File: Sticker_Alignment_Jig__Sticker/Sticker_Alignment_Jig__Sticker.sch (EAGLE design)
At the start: 5 parts

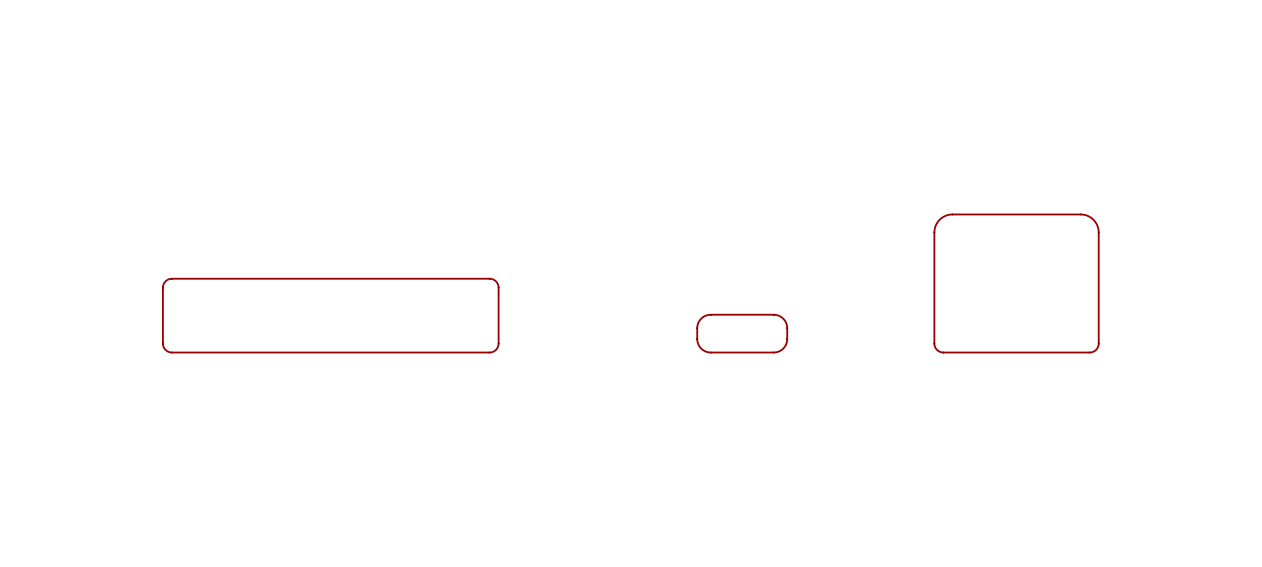
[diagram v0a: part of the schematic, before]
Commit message: Update sticker alignment jig
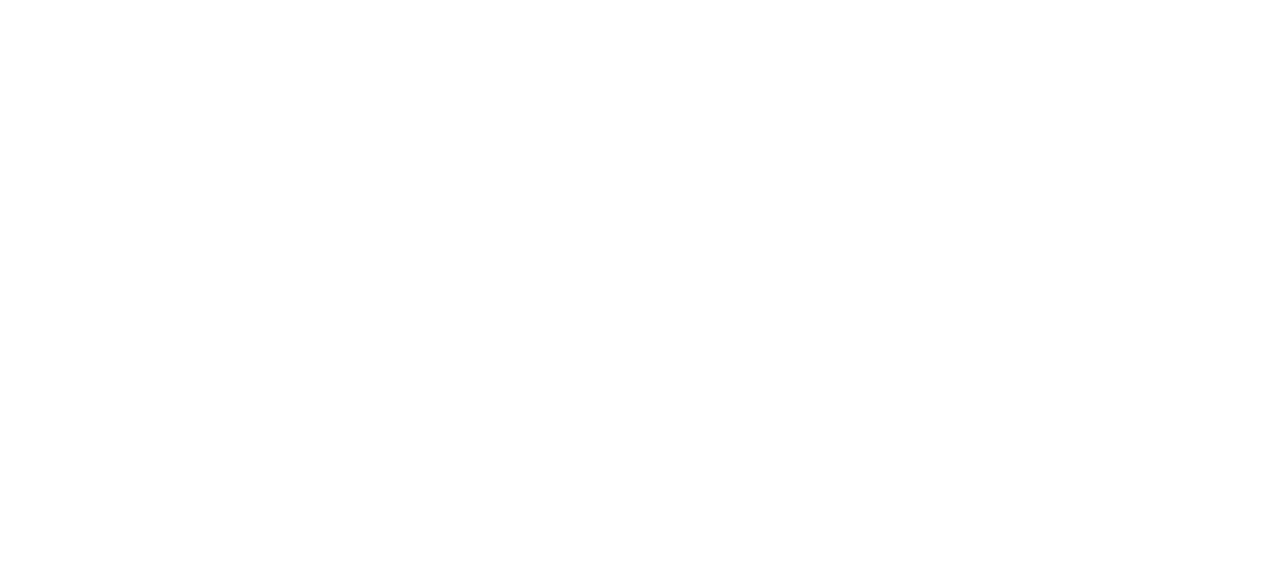
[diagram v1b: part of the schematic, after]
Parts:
- removed U$2: 3.5MM_CONNECTOR, CORS_Panels:3.5MM_CONNECTOR
- removed U$3: USB-C, CORS_Panels:USB-C
- removed U$4: ETHERNET, CORS_Panels:ETHERNET
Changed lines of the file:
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@@
 <part name="LOGO1" library="SparkFun-Aesthetics" deviceset="SFE_LOGO_NAME_FLAME" device=".3_INCH" value="SFE_LOGO_NAME_FLAME.3_INCH"/>
 <part name="FRAME1" library="SparkFun-Aesthetics" deviceset="FRAME-LETTER" device=""/>
-<part name="U$2" library="CORS_Panels" deviceset="3.5MM_CONNECTOR" device=""/>
-<part name="U$3" library="CORS_Panels" deviceset="USB-C" device=""/>
-<part name="U$4" library="CORS_Panels" deviceset="ETHERNET" device=""/>
 </parts>
 <sheets>
@@
 <attribute name="REV" x="236.22" y="6.604" size="2.7432" layer="94" font="vector"/>
 </instance>
-<instance part="U$2" gate="G$1" x="124.46" y="93.98" smashed="yes"/>
-<instance part="U$3" gate="G$1" x="170.18" y="93.98" smashed="yes"/>
-<instance part="U$4" gate="G$1" x="200.66" y="93.98" smashed="yes"/>
 </instances>
 <busses>
